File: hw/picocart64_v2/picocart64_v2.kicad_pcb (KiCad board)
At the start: 4 copper layers, 100 x 60 mm, 108 parts, among them J1 USB_C_Receptacle_USB2.0, J2 USB_C_Receptacle_USB2.0, J3 Conn_02x06_Odd_Even, J4 Micro_SD_Card_Det, J5 Conn_01x02, J6 Conn_01x06, Q1 FDN340P, SW1 BootButton, U1 LY68L6400SLIT, U10 USBLC6-2SC6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

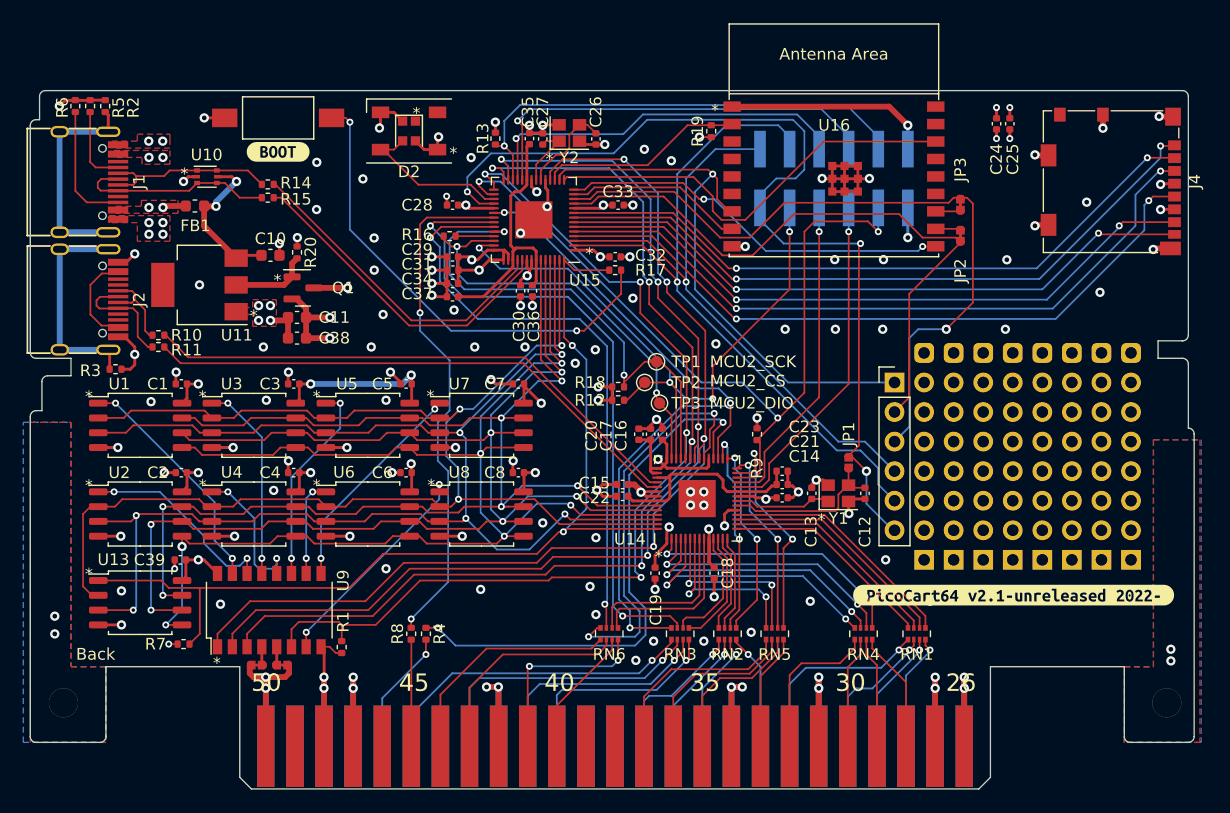
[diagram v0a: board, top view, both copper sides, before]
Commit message: Updated schematic for larger resistor arrays, removed the extra flash chip and only use the existing 8 pads, it will default to 1 for booting/loading firmware. Added a reset button to the back. Added company logo and updated text on board.
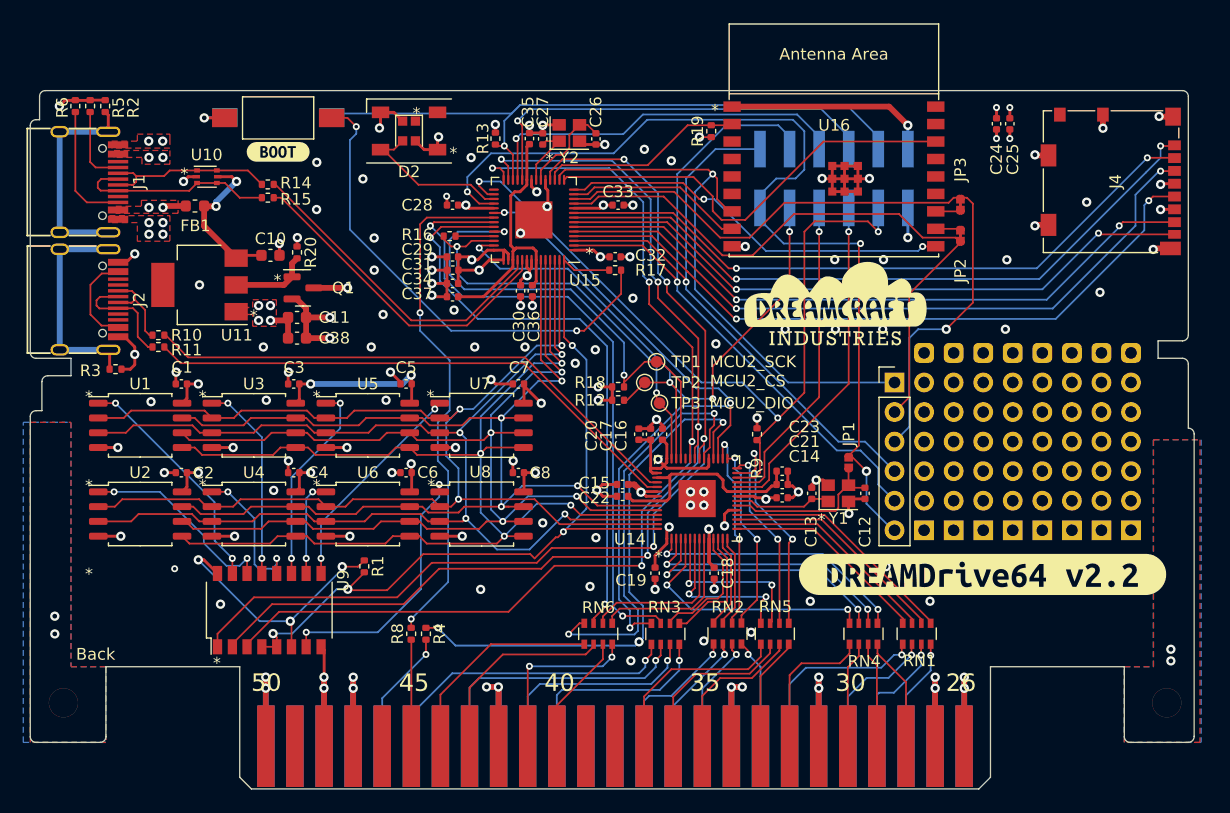
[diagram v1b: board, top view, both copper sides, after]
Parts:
- removed C39: 100n, Capacitor_SMD:C_0402_1005Metric
- removed JP4, JP5: SolderJumper_2_Bridged, picocart64:SolderJumper-2_Small_Closed
- removed R7: 10K, Resistor_SMD:R_0402_1005Metric
- removed U13: W25Q128JVS, Package_SO:SOIC-8_5.23x5.23mm_P1.27mm
- removed kibuzzard-62F9FC30: G***, kibuzzard-62F9FC30
- removed kibuzzard-62F9FC40: G***, kibuzzard-62F9FC40
- added G***: LOGO, LOGO, F.Cu at (169.1, 78.7)
- added SW2: ResetButton, Button_Switch_SMD:SW_SPST_FSMSM, B.Cu at (121.3, 62.3)
- added kibuzzard-63B14A32: G***, kibuzzard-63B14A32, B.Cu at (127.8, 105.3)
- added kibuzzard-63B14B13: G***, kibuzzard-63B14B13, F.Cu at (181.8, 101.6)
- RN1, RN2, RN3, RN4, RN5, RN6: footprint Resistor_SMD:R_Array_Convex_4x0402 -> Resistor_SMD:R_Array_Convex_4x0603
- U1, U2, U3, U4, U5, U6: value LY68L6400SLIT -> W25Q128JVS; footprint Package_SO:SOIC-8_5.275x5.275mm_P1.27mm -> Package_SO:SOIC-8_5.23x5.23mm_P1.27mm
- moved R1 7.20 mm to (128.7, 100.9)
- moved RN3 1.28 mm to (154.6, 106.7)
- moved RN6 0.95 mm to (148.8, 106.7)
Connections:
- R1 pad 1: /Mainboard/DEMUX_IE -> +3V3
- R1 pad 2: GND -> ~{SSI_CS}
- R17 pad 1: /Mainboard/~{SSI_CS} -> ~{SSI_CS}
- U14 pad 56: /Mainboard/~{SSI_CS} -> ~{SSI_CS}
- U15 pad 56: /Mainboard/~{SSI_CS} -> ~{SSI_CS}
- U4 pad 1: /PSRAM Array/CS4 -> /PSRAM Array/CS5
- U5 pad 1: /PSRAM Array/CS5 -> /PSRAM Array/CS4
- U9 pad 4: Net-(JP5-Pad2) -> ~{SSI_CS}
- U9 pad 5: Net-(JP4-Pad2) -> ~{SSI_CS}
- U9 pad 6: /Mainboard/DEMUX_IE -> +3V3
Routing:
- net /Mainboard/DEMUX_IE: track 85.2 -> 0.00 mm, vias 4 -> 0
- net /Mainboard/~{SSI_CS}: track 84.8 -> 0.00 mm, vias 2 -> 0
- net ~{SSI_CS}: track 0.00 -> 70.9 mm, vias 0 -> 4
- net /Mainboard/MCU2_RUN: track 41.1 -> 57.7 mm
- net /Mainboard/SSI_SCLK: track 116.7 -> 103.9 mm, vias 6 -> 4
- net /Mainboard/SSI_SD2: track 123.8 -> 112.6 mm, vias 6 -> 4
- net /Mainboard/SSI_SD3: track 113.4 -> 102.5 mm, vias 6 -> 4
- net /Mainboard/SSI_SD1: track 120.9 -> 110.9 mm
- net /Mainboard/SSI_SD0: track 115.4 -> 105.8 mm, vias 6 -> 4
- net +3V3: track 428.1 -> 437.0 mm, vias 32 -> 33
- net GND: track 201.0 -> 192.4 mm, vias 139 -> 134
- net /PSRAM Array/CS5: track 17.6 -> 12.6 mm
- net /PSRAM Array/CS4: track 12.6 -> 17.6 mm
- net /PSRAM Array/CS8: track 19.3 -> 22.9 mm
- net /Mainboard/~{INT1}: track 34.3 -> 36.1 mm
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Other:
- board text added: "https://github.com/khill25/Dreamdrive64 dreamcraftindustries.com"
- board text removed: "https://github.com/kbeckmann/PicoCart64 https://picoc.art/"
